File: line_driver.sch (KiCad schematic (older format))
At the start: 26 parts, among them J7 DRV632

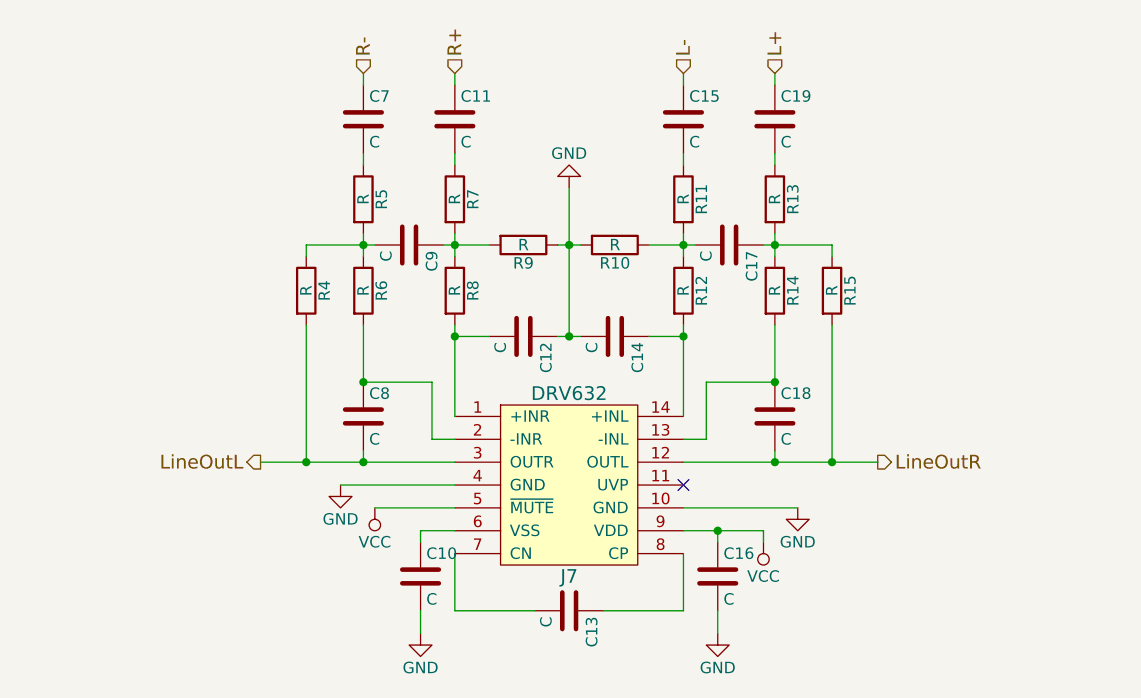
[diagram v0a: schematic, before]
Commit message: add component values and footprints.
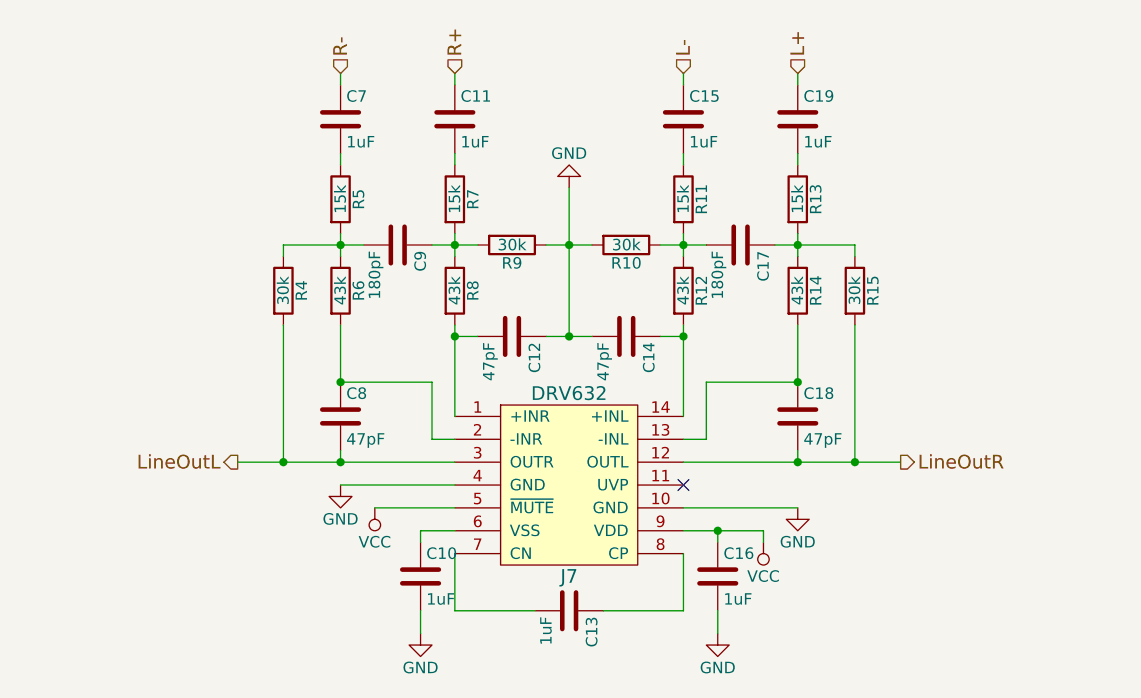
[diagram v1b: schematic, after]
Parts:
- C10, C11, C13, C15, C16, C19, C7: value C -> 1uF
- C12, C14, C18, C8: value C -> 47pF
- C17, C9: value C -> 180pF
- R10, R4, R9: value R -> 30k; footprint (none) -> Resistors_THT:R_Axial_DIN0204_L3.6mm_D1.6mm_P1.90mm_Vertical
- R11, R13, R5, R7: value R -> 15k; footprint (none) -> Resistors_THT:R_Axial_DIN0204_L3.6mm_D1.6mm_P1.90mm_Vertical
- R12, R6, R8: value R -> 43k; footprint (none) -> Resistors_THT:R_Axial_DIN0204_L3.6mm_D1.6mm_P1.90mm_Vertical
- R14: value R -> 43k
- R15: value R -> 30k
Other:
- moved on the sheet: C12, C14, C17, C18, C19, C7, C8, C9, R10, R13, R14, R15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

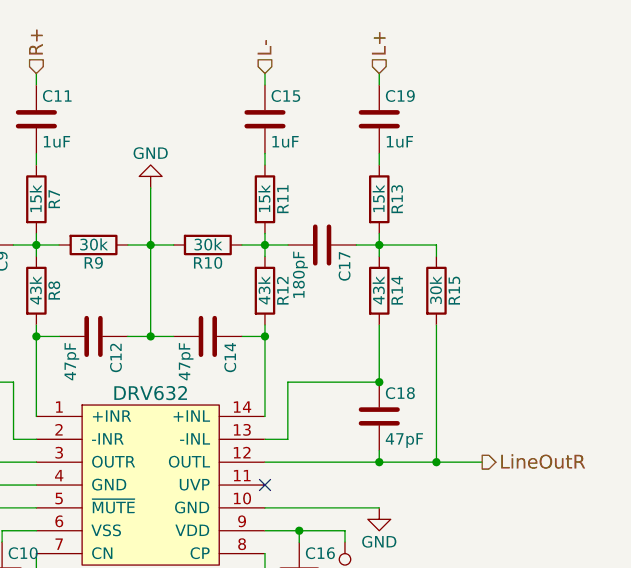
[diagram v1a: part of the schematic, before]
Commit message: Add footprints for audio switch and amp.
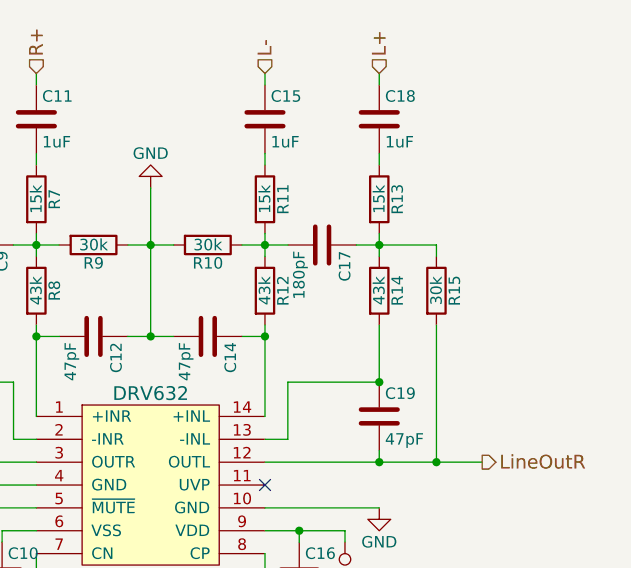
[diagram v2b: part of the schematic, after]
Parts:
- J7: footprint (none) -> blubaru:DRV632
- R14, R15: footprint (none) -> Resistors_THT:R_Axial_DIN0204_L3.6mm_D1.6mm_P1.90mm_Vertical
- renumbered C19 to C18, C18 to C19
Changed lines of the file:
@@
 LineOutL
 $Comp
-L C C18
+L C C19
 U 1 1 59179109
 P 6800 3100
-F 0 "C18" H 6825 3200 50  0000 L CNN
+F 0 "C19" H 6825 3200 50  0000 L CNN
 F 1 "47pF" H 6825 3000 50  0000 L CNN
 F 2 "" H 6838 2950 50  0001 C CNN
@@
 	5300 1950 5300 2000
 $Comp
-L C C19
+L C C18
 U 1 1 5917A4E1
 P 6800 1800
-F 0 "C19" H 6825 1900 50  0000 L CNN
+F 0 "C18" H 6825 1900 50  0000 L CNN
 F 1 "1uF" H 6825 1700 50  0000 L CNN
 F 2 "" H 6838 1650 50  0001 C CNN
@@
 F 0 "R14" V 6880 2550 50  0000 C CNN
 F 1 "43k" V 6800 2550 50  0000 C CNN
-F 2 "" V 6730 2550 50  0001 C CNN
+F 2 "Resistors_THT:R_Axial_DIN0204_L3.6mm_D1.6mm_P1.90mm_Vertical" V 6730 2550 50  0001 C CNN
 F 3 "" H 6800 2550 50  0001 C CNN
 	1    6800 2550
@@
 F 0 "R15" V 7130 2550 50  0000 C CNN
 F 1 "30k" V 7050 2550 50  0000 C CNN
-F 2 "" V 6980 2550 50  0001 C CNN
+F 2 "Resistors_THT:R_Axial_DIN0204_L3.6mm_D1.6mm_P1.90mm_Vertical" V 6980 2550 50  0001 C CNN
 F 3 "" H 7050 2550 50  0001 C CNN
 	1    7050 2550
@@
 F 0 "J7" H 5800 2200 60  0000 C CNN
 F 1 "DRV632" H 5800 3000 60  0000 C CNN
-F 2 "" H 5800 3000 60  0001 C CNN
+F 2 "blubaru:DRV632" H 5800 3000 60  0001 C CNN
 F 3 "http://www.ti.com/lit/ds/symlink/drv632.pdf" H 5800 3000 60  0001 C CNN
 	1    5800 3000

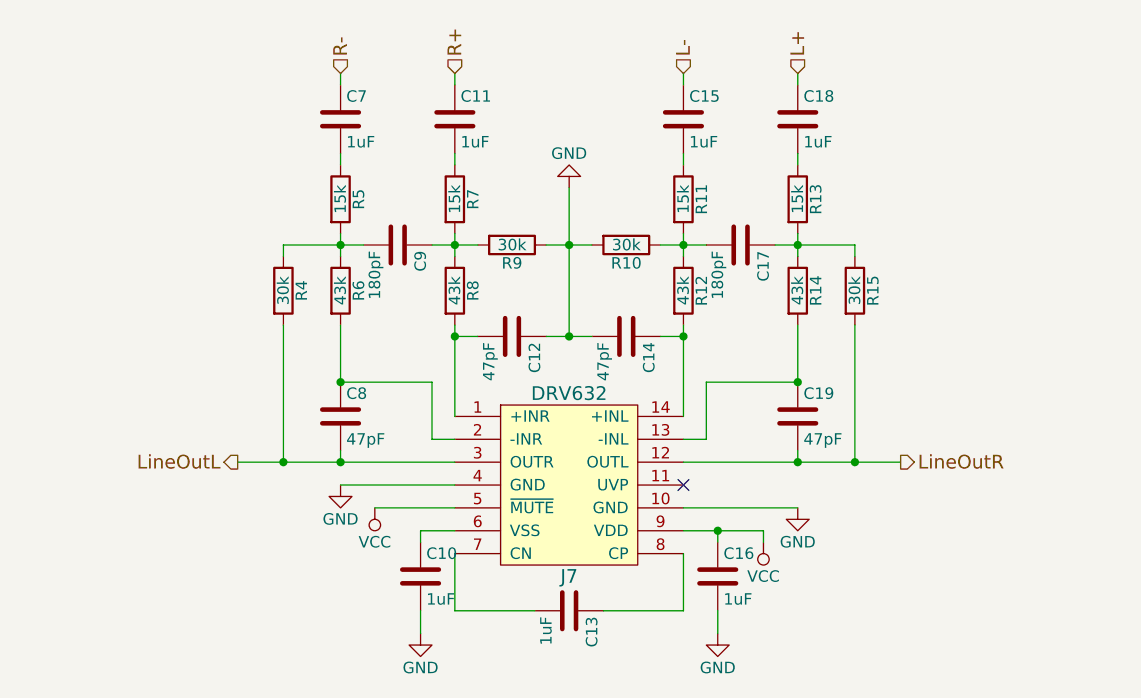
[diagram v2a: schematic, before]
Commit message: Add RC filter on line-outs, matching the EVM.
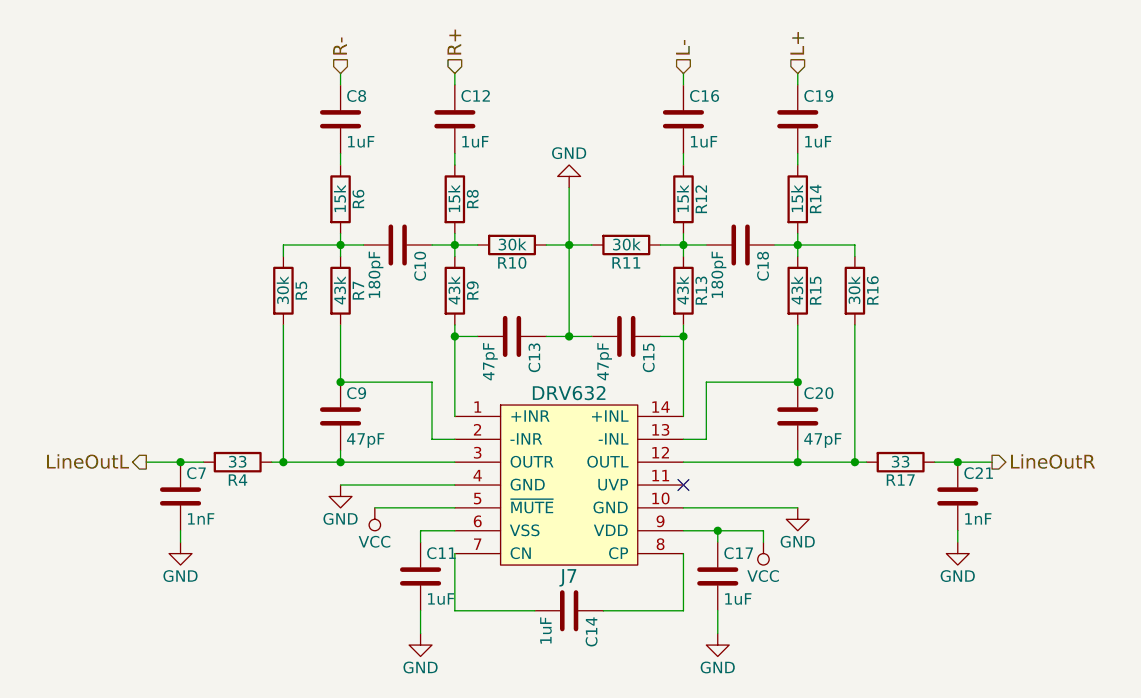
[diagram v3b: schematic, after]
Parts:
- added C21, C7: 1nF, symbol C
- added R17, R4: 33, symbol R
- renumbered C9 to C10, C10 to C11, C11 to C12, C12 to C13, C13 to C14, C14 to C15, C15 to C16, C16 to C17, C17 to C18, C18 to C19, C19 to C20, C7 to C8, C8 to C9, R9 to R10, R10 to R11, R11 to R12, R12 to R13, R13 to R14, R14 to R15, R15 to R16, R4 to R5, R5 to R6, R6 to R7, R7 to R8, R8 to R9
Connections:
- net GND: now also C21.2, C7.2
- net LineOutL: now also C7.1, R4.2; no longer C9.2, J7.3 (OUTR), R5.2
- net LineOutR: now also C21.1, R17.1; no longer C20.2, J7.12 (OUTL), R16.2
- new net: C20.2, J7.12 (OUTL), R16.2, R17.2
- new net: C9.2, J7.3 (OUTR), R4.1, R5.2
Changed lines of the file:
@@
 $EndComp
 $Comp
-L C C13
+L C C14
 U 1 1 59178EA2
 P 5800 3950
-F 0 "C13" H 5825 4050 50  0000 L CNN
+F 0 "C14" H 5825 4050 50  0000 L CNN
 F 1 "1uF" H 5825 3850 50  0000 L CNN
 F 2 "" H 5838 3800 50  0001 C CNN
@@
 	6300 3500 6800 3500
 $Comp
-L C C10
+L C C11
 U 1 1 59178EFD
 P 5150 3800
-F 0 "C10" H 5175 3900 50  0000 L CNN
+F 0 "C11" H 5175 3900 50  0000 L CNN
 F 1 "1uF" H 5175 3700 50  0000 L CNN
 F 2 "" H 5188 3650 50  0001 C CNN
@@
 	5150 3950 5150 4050
 $Comp
-L C C16
+L C C17
 U 1 1 59178FC9
 P 6450 3800
-F 0 "C16" H 6475 3900 50  0000 L CNN
+F 0 "C17" H 6475 3900 50  0000 L CNN
 F 1 "1uF" H 6475 3700 50  0000 L CNN
 F 2 "" H 6488 3650 50  0001 C CNN
@@
 NoConn ~ 6300 3400
 Wire Wire Line
-	6300 3300 7250 3300
-Wire Wire Line
-	4350 3300 5300 3300
-Text HLabel 7250 3300 2    60   Output ~ 0
+	6300 3300 7100 3300
+Wire Wire Line
+	4500 3300 5300 3300
+Text HLabel 7650 3300 2    60   Output ~ 0
 LineOutR
-Text HLabel 4350 3300 0    60   Output ~ 0
+Text HLabel 3950 3300 0    60   Output ~ 0
 LineOutL
 $Comp
-L C C19
+L C C20
 U 1 1 59179109
 P 6800 3100
-F 0 "C19" H 6825 3200 50  0000 L CNN
+F 0 "C20" H 6825 3200 50  0000 L CNN
 F 1 "47pF" H 6825 3000 50  0000 L CNN
 F 2 "" H 6838 2950 50  0001 C CNN
@@
 $EndComp
 $Comp
-L C C8
+L C C9
 U 1 1 5917915A
 P 4800 3100
-F 0 "C8" H 4825 3200 50  0000 L CNN
+F 0 "C9" H 4825 3200 50  0000 L CNN
 F 1 "47pF" H 4825 3000 50  0000 L CNN
 F 2 "" H 4838 2950 50  0001 C CNN
@@
 	6400 3200 6300 3200
 $Comp
-L C C14
+L C C15
 U 1 1 591791B6
 P 6050 2750
-F 0 "C14" H 6075 2850 50  0000 L CNN
+F 0 "C15" H 6075 2850 50  0000 L CNN
 F 1 "47pF" H 6075 2650 50  0000 L CNN
 F 2 "" H 6088 2600 50  0001 C CNN
@@
 $EndComp
 $Comp
-L C C12
+L C C13
 U 1 1 591791EB
 P 5550 2750
-F 0 "C12" H 5575 2850 50  0000 L CNN
+F 0 "C13" H 5575 2850 50  0000 L CNN
 F 1 "47pF" H 5575 2650 50  0000 L CNN
 F 2 "" H 5588 2600 50  0001 C CNN
@@
 $EndComp
 $Comp
-L R R9
+L R R10
 U 1 1 59179216
 P 5550 2350
-F 0 "R9" V 5630 2350 50  0000 C CNN
+F 0 "R10" V 5630 2350 50  0000 C CNN
 F 1 "30k" V 5550 2350 50  0000 C CNN
 F 2 "Resistors_THT:R_Axial_DIN0204_L3.6mm_D1.6mm_P1.90mm_Vertical" V 5480 2350 50  0001 C CNN
@@
 $EndComp
 $Comp
-L R R10
+L R R11
 U 1 1 59179241
 P 6050 2350
-F 0 "R10" V 6130 2350 50  0000 C CNN
+F 0 "R11" V 6130 2350 50  0000 C CNN
 F 1 "30k" V 6050 2350 50  0000 C CNN
 F 2 "Resistors_THT:R_Axial_DIN0204_L3.6mm_D1.6mm_P1.90mm_Vertical" V 5980 2350 50  0001 C CNN
@@
 Connection ~ 5800 2350
 $Comp
-L R R12
+L R R13
 U 1 1 59179384
 P 6300 2550
-F 0 "R12" V 6380 2550 50  0000 C CNN
+F 0 "R13" V 6380 2550 50  0000 C CNN
 F 1 "43k" V 6300 2550 50  0000 C CNN
 F 2 "Resistors_THT:R_Axial_DIN0204_L3.6mm_D1.6mm_P1.90mm_Vertical" V 6230 2550 50  0001 C CNN
@@
 $EndComp
 $Comp
-L R R8
+L R R9
 U 1 1 591793C1
 P 5300 2550
-F 0 "R8" V 5380 2550 50  0000 C CNN
+F 0 "R9" V 5380 2550 50  0000 C CNN
 F 1 "43k" V 5300 2550 50  0000 C CNN
 F 2 "Resistors_THT:R_Axial_DIN0204_L3.6mm_D1.6mm_P1.90mm_Vertical" V 5230 2550 50  0001 C CNN
@@
 	5300 2700 5300 3100
 $Comp
-L R R11
+L R R12
 U 1 1 5917A21C
 P 6300 2150
-F 0 "R11" V 6380 2150 50  0000 C CNN
+F 0 "R12" V 6380 2150 50  0000 C CNN
 F 1 "15k" V 6300 2150 50  0000 C CNN
 F 2 "Resistors_THT:R_Axial_DIN0204_L3.6mm_D1.6mm_P1.90mm_Vertical" V 6230 2150 50  0001 C CNN
@@
 $EndComp
 $Comp
-L R R7
+L R R8
 U 1 1 5917A253
 P 5300 2150
-F 0 "R7" V 5380 2150 50  0000 C CNN
+F 0 "R8" V 5380 2150 50  0000 C CNN
 F 1 "15k" V 5300 2150 50  0000 C CNN
 F 2 "Resistors_THT:R_Axial_DIN0204_L3.6mm_D1.6mm_P1.90mm_Vertical" V 5230 2150 50  0001 C CNN
@@
 Connection ~ 6300 2350
 $Comp
-L C C15
+L C C16
 U 1 1 5917A3EF
 P 6300 1800
-F 0 "C15" H 6325 1900 50  0000 L CNN
+F 0 "C16" H 6325 1900 50  0000 L CNN
 F 1 "1uF" H 6325 1700 50  0000 L CNN
 F 2 "" H 6338 1650 50  0001 C CNN
@@
 $EndComp
 $Comp
-L C C11
+L C C12
 U 1 1 5917A42E
 P 5300 1800
-F 0 "C11" H 5325 1900 50  0000 L CNN
+F 0 "C12" H 5325 1900 50  0000 L CNN
 F 1 "1uF" H 5325 1700 50  0000 L CNN
 F 2 "" H 5338 1650 50  0001 C CNN
@@
 	5300 1950 5300 2000
 $Comp
-L C C18
+L C C19
 U 1 1 5917A4E1
 P 6800 1800
-F 0 "C18" H 6825 1900 50  0000 L CNN
+F 0 "C19" H 6825 1900 50  0000 L CNN
 F 1 "1uF" H 6825 1700 50  0000 L CNN
 F 2 "" H 6838 1650 50  0001 C CNN
@@
 $EndComp
 $Comp
-L C C7
+L C C8
 U 1 1 5917A52C
 P 4800 1800
-F 0 "C7" H 4825 1900 50  0000 L CNN
+F 0 "C8" H 4825 1900 50  0000 L CNN
 F 1 "1uF" H 4825 1700 50  0000 L CNN
 F 2 "" H 4838 1650 50  0001 C CNN
@@
 $EndComp
 $Comp
-L C C9
+L C C10
 U 1 1 5917A56B
 P 5050 2350
-F 0 "C9" H 5075 2450 50  0000 L CNN
+F 0 "C10" H 5075 2450 50  0000 L CNN
 F 1 "180pF" H 5075 2250 50  0000 L CNN
 F 2 "" H 5088 2200 50  0001 C CNN
@@
 $EndComp
 $Comp
-L C C17
+L C C18
 U 1 1 5917A5AC
 P 6550 2350
-F 0 "C17" H 6575 2450 50  0000 L CNN
+F 0 "C18" H 6575 2450 50  0000 L CNN
 F 1 "180pF" H 6575 2250 50  0000 L CNN
 F 2 "" H 6588 2200 50  0001 C CNN
@@
 	6700 2350 7050 2350
 $Comp
-L R R14
+L R R15
 U 1 1 5917A8A8
 P 6800 2550
-F 0 "R14" V 6880 2550 50  0000 C CNN
+F 0 "R15" V 6880 2550 50  0000 C CNN
 F 1 "43k" V 6800 2550 50  0000 C CNN
 F 2 "Resistors_THT:R_Axial_DIN0204_L3.6mm_D1.6mm_P1.90mm_Vertical" V 6730 2550 50  0001 C CNN
@@
 $EndComp
 $Comp
-L R R6
+L R R7
 U 1 1 5917A8FF
 P 4800 2550
-F 0 "R6" V 4880 2550 50  0000 C CNN
+F 0 "R7" V 4880 2550 50  0000 C CNN
 F 1 "43k" V 4800 2550 50  0000 C CNN
 F 2 "Resistors_THT:R_Axial_DIN0204_L3.6mm_D1.6mm_P1.90mm_Vertical" V 4730 2550 50  0001 C CNN
@@
 Connection ~ 4800 2350
 $Comp
-L R R13
+L R R14
 U 1 1 5917AA6A
 P 6800 2150
-F 0 "R13" V 6880 2150 50  0000 C CNN
+F 0 "R14" V 6880 2150 50  0000 C CNN
 F 1 "15k" V 6800 2150 50  0000 C CNN
 F 2 "Resistors_THT:R_Axial_DIN0204_L3.6mm_D1.6mm_P1.90mm_Vertical" V 6730 2150 50  0001 C CNN
@@
 $EndComp
 $Comp
-L R R5
+L R R6
 U 1 1 5917AAD3
 P 4800 2150
-F 0 "R5" V 4880 2150 50  0000 C CNN
+F 0 "R6" V 4880 2150 50  0000 C CNN
 F 1 "15k" V 4800 2150 50  0000 C CNN
 F 2 "Resistors_THT:R_Axial_DIN0204_L3.6mm_D1.6mm_P1.90mm_Vertical" V 4730 2150 50  0001 C CNN
@@
 Connection ~ 4800 2950
 $Comp
-L R R15
+L R R16
 U 1 1 5917AD17
 P 7050 2550
-F 0 "R15" V 7130 2550 50  0000 C CNN
+F 0 "R16" V 7130 2550 50  0000 C CNN
 F 1 "30k" V 7050 2550 50  0000 C CNN
 F 2 "Resistors_THT:R_Axial_DIN0204_L3.6mm_D1.6mm_P1.90mm_Vertical" V 6980 2550 50  0001 C CNN
@@
 $EndComp
 $Comp
-L R R4
+L R R5
 U 1 1 5917AD78
 P 4550 2550
-F 0 "R4" V 4630 2550 50  0000 C CNN
+F 0 "R5" V 4630 2550 50  0000 C CNN
 F 1 "30k" V 4550 2550 50  0000 C CNN
 F 2 "Resistors_THT:R_Axial_DIN0204_L3.6mm_D1.6mm_P1.90mm_Vertical" V 4480 2550 50  0001 C CNN
@@
 	1    0    0    -1
 $EndComp
+$Comp
+L C C21
+U 1 1 5933924A
+P 7500 3450
+F 0 "C21" H 7525 3550 50  0000 L CNN
+F 1 "1nF" H 7525 3350 50  0000 L CNN
+F 2 "" H 7538 3300 50  0001 C CNN
+F 3 "" H 7500 3450 50  0001 C CNN
+	1    7500 3450
+	1    0    0    -1
+$EndComp
+$Comp
+L C C7
+U 1 1 593392DF
+P 4100 3450
+F 0 "C7" H 4125 3550 50  0000 L CNN
+F 1 "1nF" H 4125 3350 50  0000 L CNN
+F 2 "" H 4138 3300 50  0001 C CNN
+F 3 "" H 4100 3450 50  0001 C CNN
+	1    4100 3450
+	1    0    0    -1
+$EndComp
+$Comp
+L R R17
+U 1 1 59339334
+P 7250 3300
+F 0 "R17" V 7330 3300 50  0000 C CNN
+F 1 "33" V 7250 3300 50  0000 C CNN
+F 2 "" V 7180 3300 50  0001 C CNN
+F 3 "" H 7250 3300 50  0001 C CNN
+	1    7250 3300
+	0    1    1    0
+$EndComp
+$Comp
+L R R4
+U 1 1 593393C3
+P 4350 3300
+F 0 "R4" V 4430 3300 50  0000 C CNN
+F 1 "33" V 4350 3300 50  0000 C CNN
+F 2 "" V 4280 3300 50  0001 C CNN
+F 3 "" H 4350 3300 50  0001 C CNN
+	1    4350 3300
+	0    1    1    0
+$EndComp
+Wire Wire Line
+	7400 3300 7650 3300
+Wire Wire Line
+	3950 3300 4200 3300
+Connection ~ 7500 3300
+Connection ~ 4100 3300
+$Comp
+L GND #PWR030
+U 1 1 59339996
+P 7500 3650
+F 0 "#PWR030" H 7500 3400 50  0001 C CNN
+F 1 "GND" H 7500 3500 50  0000 C CNN
+F 2 "" H 7500 3650 50  0001 C CNN
+F 3 "" H 7500 3650 50  0001 C CNN
+	1    7500 3650
+	1    0    0    -1
+$EndComp
+$Comp
+L GND #PWR031
+U 1 1 593399E6
+P 4100 3650
+F 0 "#PWR031" H 4100 3400 50  0001 C CNN
+F 1 "GND" H 4100 3500 50  0000 C CNN
+F 2 "" H 4100 3650 50  0001 C CNN
+F 3 "" H 4100 3650 50  0001 C CNN
+	1    4100 3650
+	1    0    0    -1
+$EndComp
+Wire Wire Line
+	7500 3600 7500 3650
+Wire Wire Line
+	4100 3600 4100 3650
 $EndSCHEMATC

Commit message: Adjust some cap prefixes and add large CD/Stereo labels to top level pages.
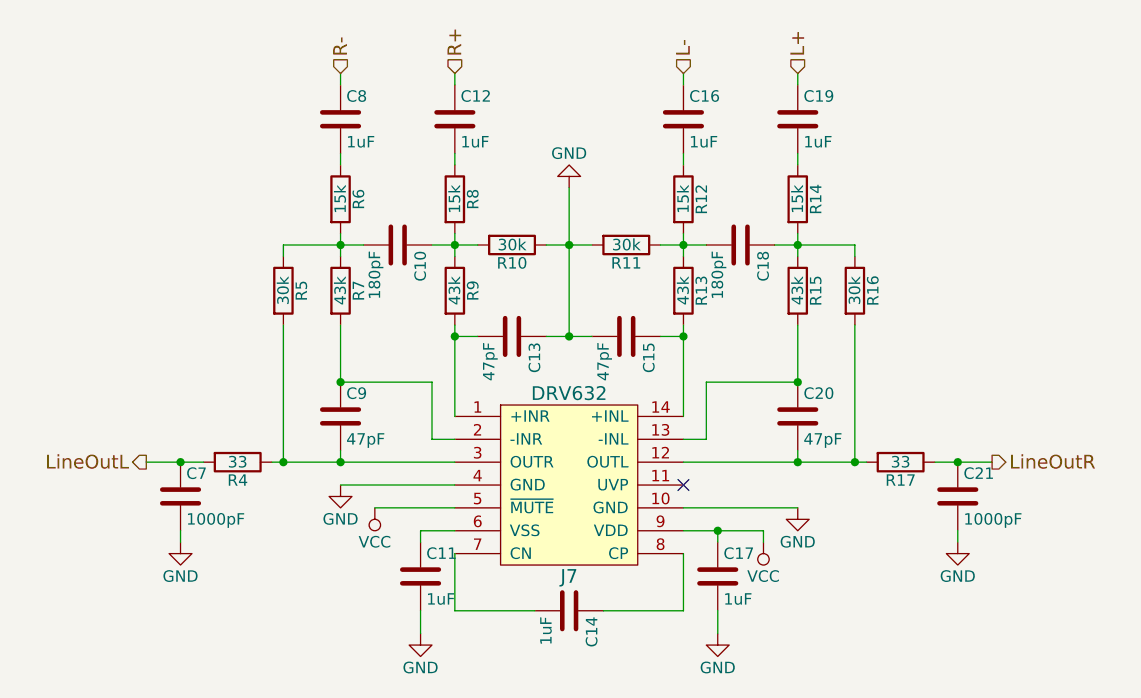
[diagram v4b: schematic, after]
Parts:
- C21, C7: value 1nF -> 1000pF
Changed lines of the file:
@@
 P 7500 3450
 F 0 "C21" H 7525 3550 50  0000 L CNN
-F 1 "1nF" H 7525 3350 50  0000 L CNN
+F 1 "1000pF" H 7525 3350 50  0000 L CNN
 F 2 "" H 7538 3300 50  0001 C CNN
 F 3 "" H 7500 3450 50  0001 C CNN
@@
 P 4100 3450
 F 0 "C7" H 4125 3550 50  0000 L CNN
-F 1 "1nF" H 4125 3350 50  0000 L CNN
+F 1 "1000pF" H 4125 3350 50  0000 L CNN
 F 2 "" H 4138 3300 50  0001 C CNN
 F 3 "" H 4100 3450 50  0001 C CNN
